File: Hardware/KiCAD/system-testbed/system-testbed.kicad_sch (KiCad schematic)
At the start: 11 parts, among them J2 Stemma QT, J3 Stemma QT, X4 EYESPI, X5 EYESPI, X6 EYESPI, X7 EYESPI, X8 EYESPI

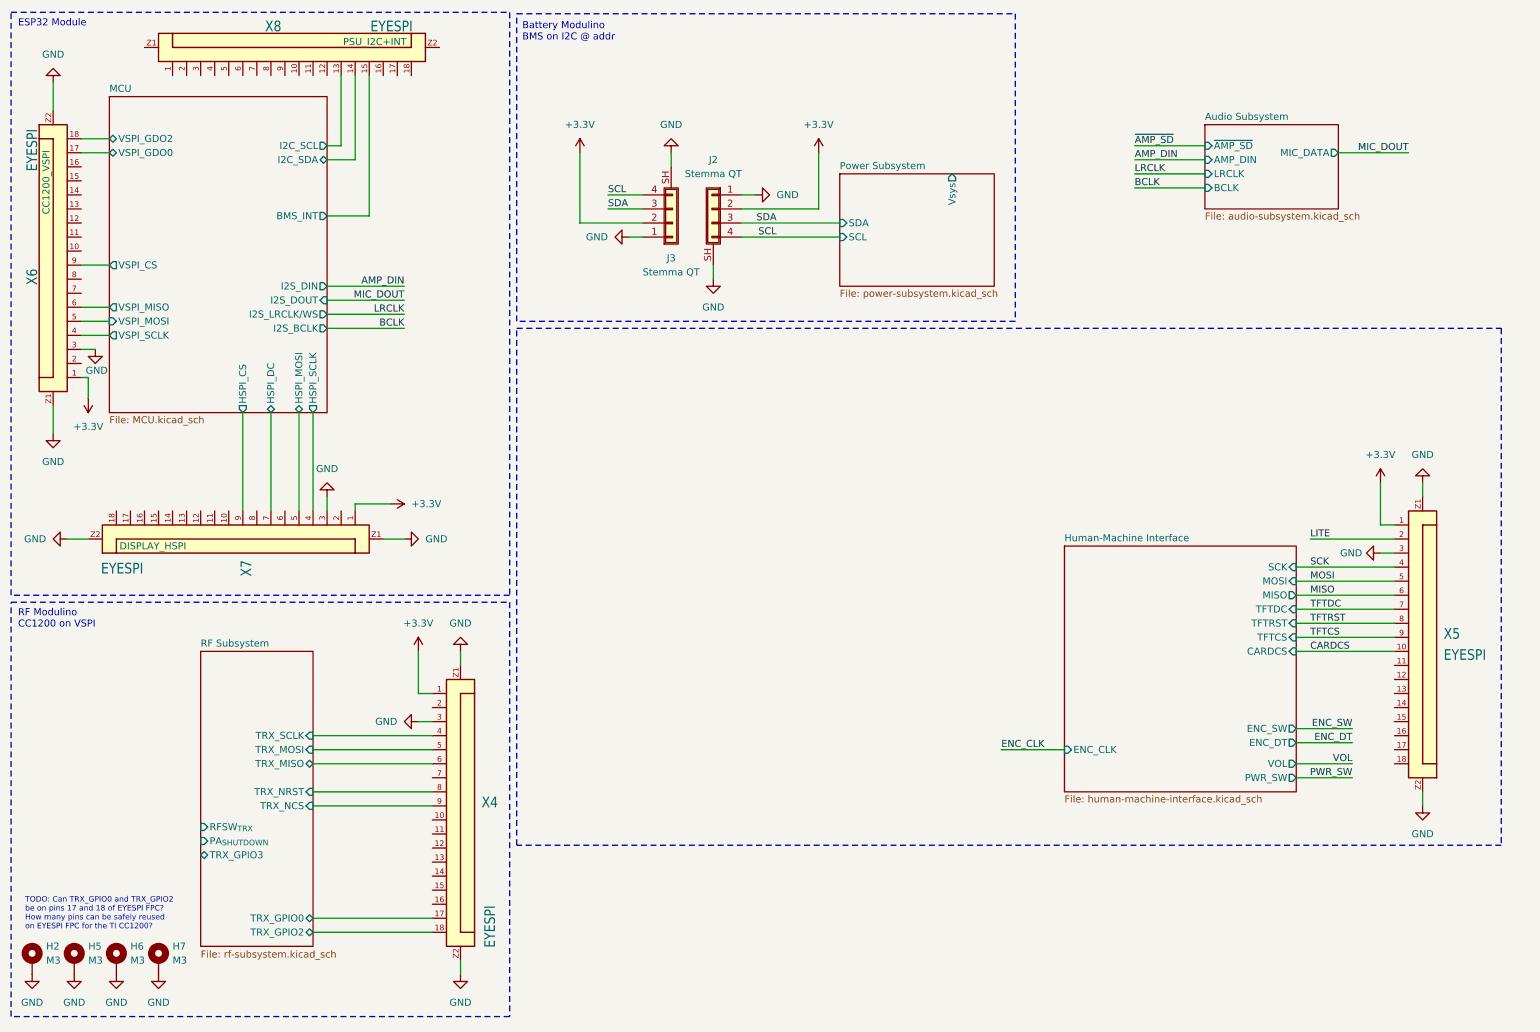
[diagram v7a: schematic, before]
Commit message: fix: allow for DRC use in PCB editor by successful reannotation
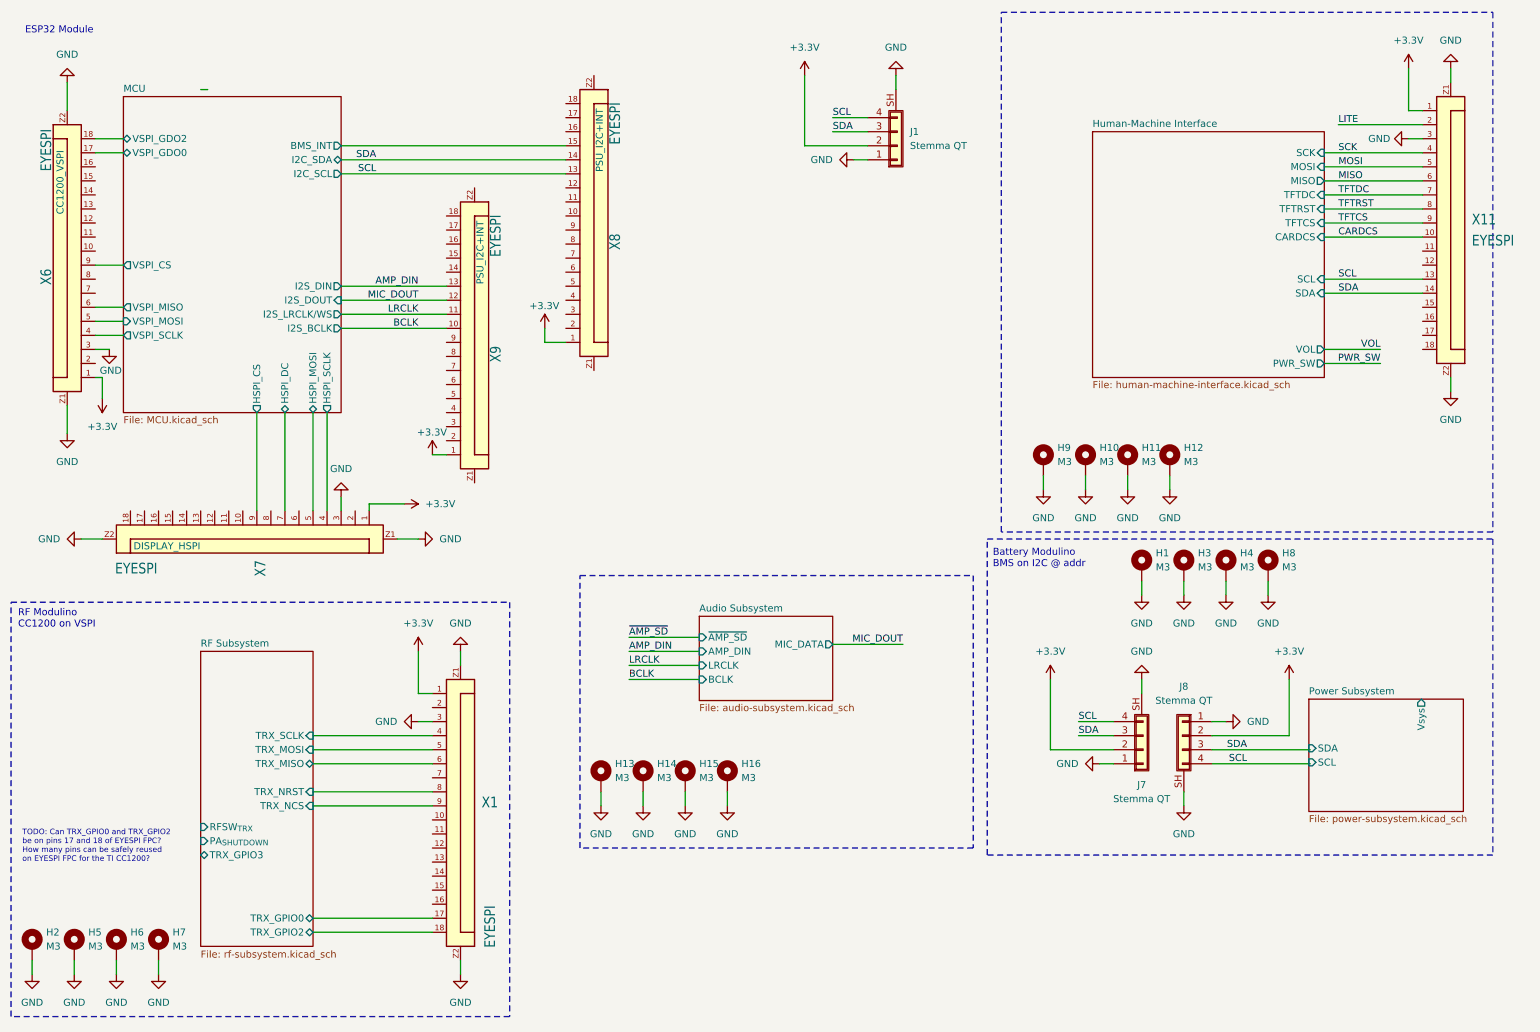
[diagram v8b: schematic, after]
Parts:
- removed J2, J3: Stemma QT, Connector_JST:JST_SH_SM04B-SRSS-TB_1x04-1MP_P1.00mm_Horizontal, symbol Connector_Generic_Shielded:Conn_01x04_Shielded
- removed X5: EYESPI, capstone-project:Adafruit EYESPI FPC Connector, symbol capstone-project:Adafruit EYESPI FPC Connector
- added H1, H10, H11, H12, H13, H14, H15, H16, H3, H4, H8, H9: M3, MountingHole:MountingHole_3.2mm_M3_ISO14580_Pad, symbol Mechanical:MountingHole_Pad
- added J1, J7, J8: Stemma QT, Connector_JST:JST_SH_SM04B-SRSS-TB_1x04-1MP_P1.00mm_Horizontal, symbol Connector_Generic_Shielded:Conn_01x04_Shielded
- added X11, X9: EYESPI, capstone-project:Adafruit EYESPI FPC Connector, symbol capstone-project:Adafruit EYESPI FPC Connector
- X1: renamed from X4; Assignment (none) -> CC1200_VSPI
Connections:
- net MCU/I2C_SCL is gone; now on net SCL: X8.13
- net MCU/I2C_SDA is gone; now on net SDA: X8.14
- net +3.3V: now also X8.1, J1.2 (Pin_2), J7.2 (Pin_2), J8.2 (Pin_2), X11.1, X9.1
- net AMP_DIN: now also X9.13
- net BCLK: now also X9.10
- net CARDCS: now also X11.10
- net GND: now also H1.1, H10.1, H11.1, H12.1, H13.1, H14.1, H15.1, H16.1, H3.1, H4.1, H8.1, H9.1, J1.1 (Pin_1), J1.SH (Shield), J7.1 (Pin_1), J7.SH (Shield), J8.1 (Pin_1), J8.SH (Shield), X11.3, X11.Z1, X11.Z2
- net LITE: now also X11.2
- net LRCLK: now also X9.11
- net MIC_DOUT: now also X9.12
- net MISO: now also X11.6
- net MOSI: now also X11.5
- net SCK: now also X11.4
- net SCL: now also J1.4 (Pin_4), J7.4 (Pin_4), J8.4 (Pin_4), X11.13
- net SDA: now also J1.3 (Pin_3), J7.3 (Pin_3), J8.3 (Pin_3), X11.14
- net TFTCS: now also X11.9
- net TFTDC: now also X11.7
- net TFTRST: now also X11.8
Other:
- sheet Human-Machine Interface ports: added SCL, SDA; removed ENC_CLK, ENC_DT, ENC_SW
- moved on the sheet: H2, H5, H6, H7, X6, X7, X8
